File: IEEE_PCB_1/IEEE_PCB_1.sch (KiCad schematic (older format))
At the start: 24 parts, among them U1 555, U2 4017

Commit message: Rev2
Made more changes to the schematic. Will start the footprints soon
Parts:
- added U3: EG1218, symbol IEEE_PCB_Ornament:EG1218
- added U4: 1058TR, symbol IEEE_PCB_Ornament:1058TR
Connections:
- net +3V3: now also U3.1
- net GND: now also U3.3, U4.2 (GND)
- new net: U3.2, U4.1 (PWR)
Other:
- note added: "Clock Circuit"
- note added: "LED circuit"
- note added: "Power"
- moved on the sheet: C1, C2, D1, D2, D3, D4, D5, D6, D7, D8, D9, R1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

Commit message: Footprint assignment
assigned the custom symbols with the custom symbols. Still waiting for standard parts
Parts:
- U1: footprint (none) -> IEEE_PCB_Ornament:555
- U2: footprint (none) -> IEEE_PCB_Ornament:4017
- U3: footprint (none) -> IEEE_PCB_Ornament:EG1218
- U4: footprint (none) -> IEEE_PCB_Ornament:1058TR
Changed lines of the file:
@@
 F 0 "U2" H 3750 3775 50  0000 C CNN
 F 1 "4017" H 3750 3684 50  0000 C CNN
-F 2 "" H 3800 3250 50  0001 C CNN
+F 2 "IEEE_PCB_Ornament:4017" H 3800 3250 50  0001 C CNN
 F 3 "" H 3800 3250 50  0001 C CNN
 	1    3750 3250
@@
 F 0 "U4" H 8750 5500 50  0000 C CNN
 F 1 "1058TR" H 8750 5350 50  0000 C CNN
-F 2 "" H 8750 5400 50  0001 C CNN
+F 2 "IEEE_PCB_Ornament:1058TR" H 8750 5400 50  0001 C CNN
 F 3 "" H 8750 5400 50  0001 C CNN
 	1    8750 5050
@@
 F 0 "U3" V 9254 4522 50  0000 R CNN
 F 1 "EG1218" V 9345 4522 50  0000 R CNN
-F 2 "" H 9300 5000 50  0001 C CNN
+F 2 "IEEE_PCB_Ornament:EG1218" H 9300 5000 50  0001 C CNN
 F 3 "" H 9300 5000 50  0001 C CNN
 	1    9300 4900
@@
 F 0 "U1" H 9250 1965 50  0000 C CNN
 F 1 "555" H 9250 1874 50  0000 C CNN
-F 2 "" H 9200 1150 50  0001 C CNN
+F 2 "IEEE_PCB_Ornament:555" H 9200 1150 50  0001 C CNN
 F 3 "" H 9200 1150 50  0001 C CNN
 	1    9200 1600

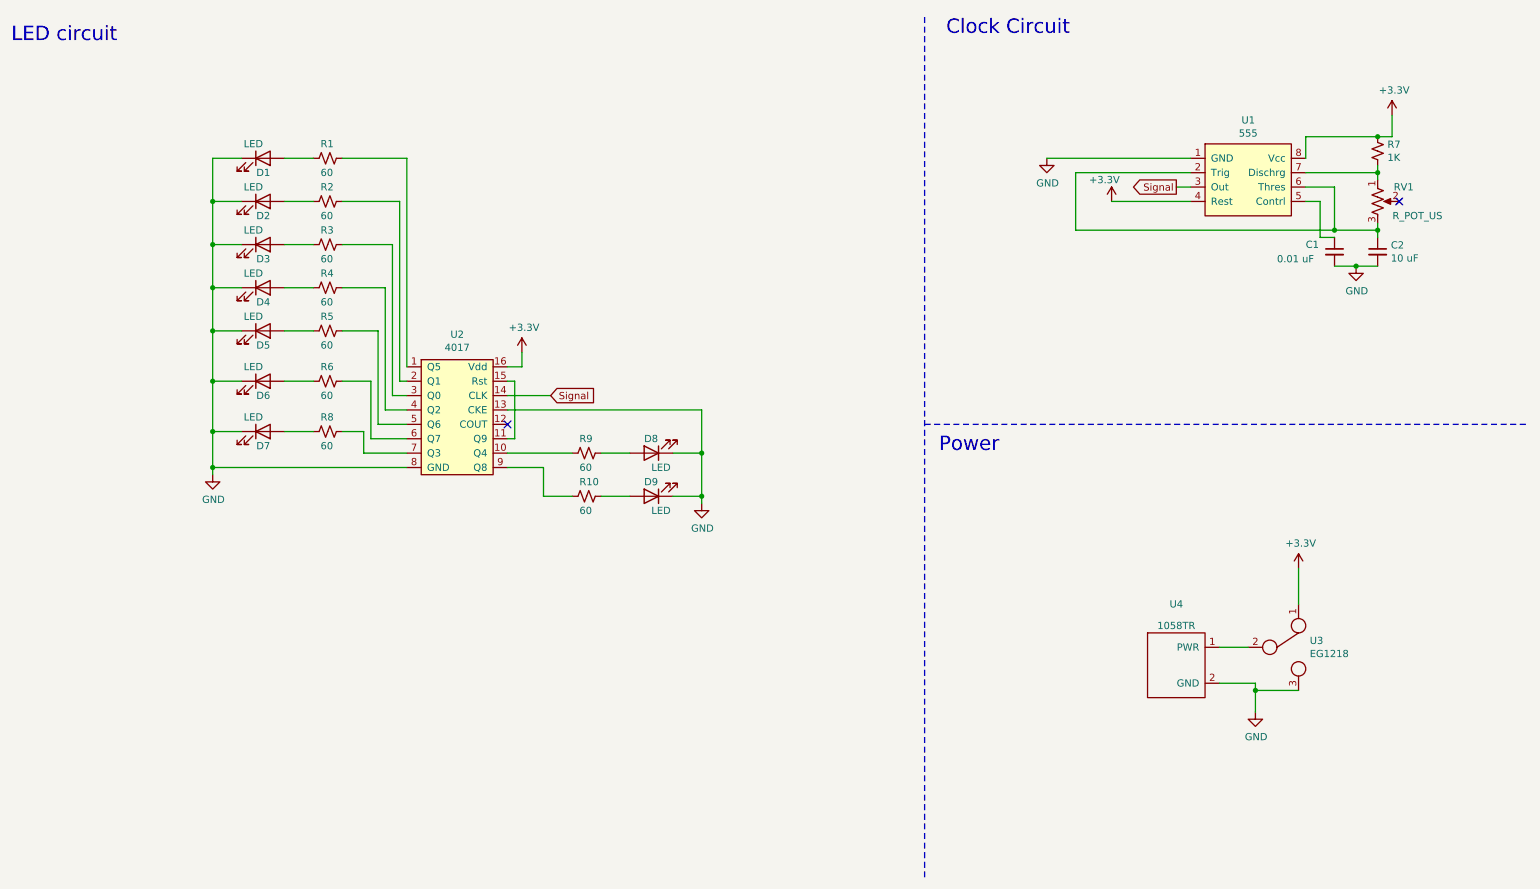
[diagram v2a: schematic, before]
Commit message: Rev3
editted the LEDs
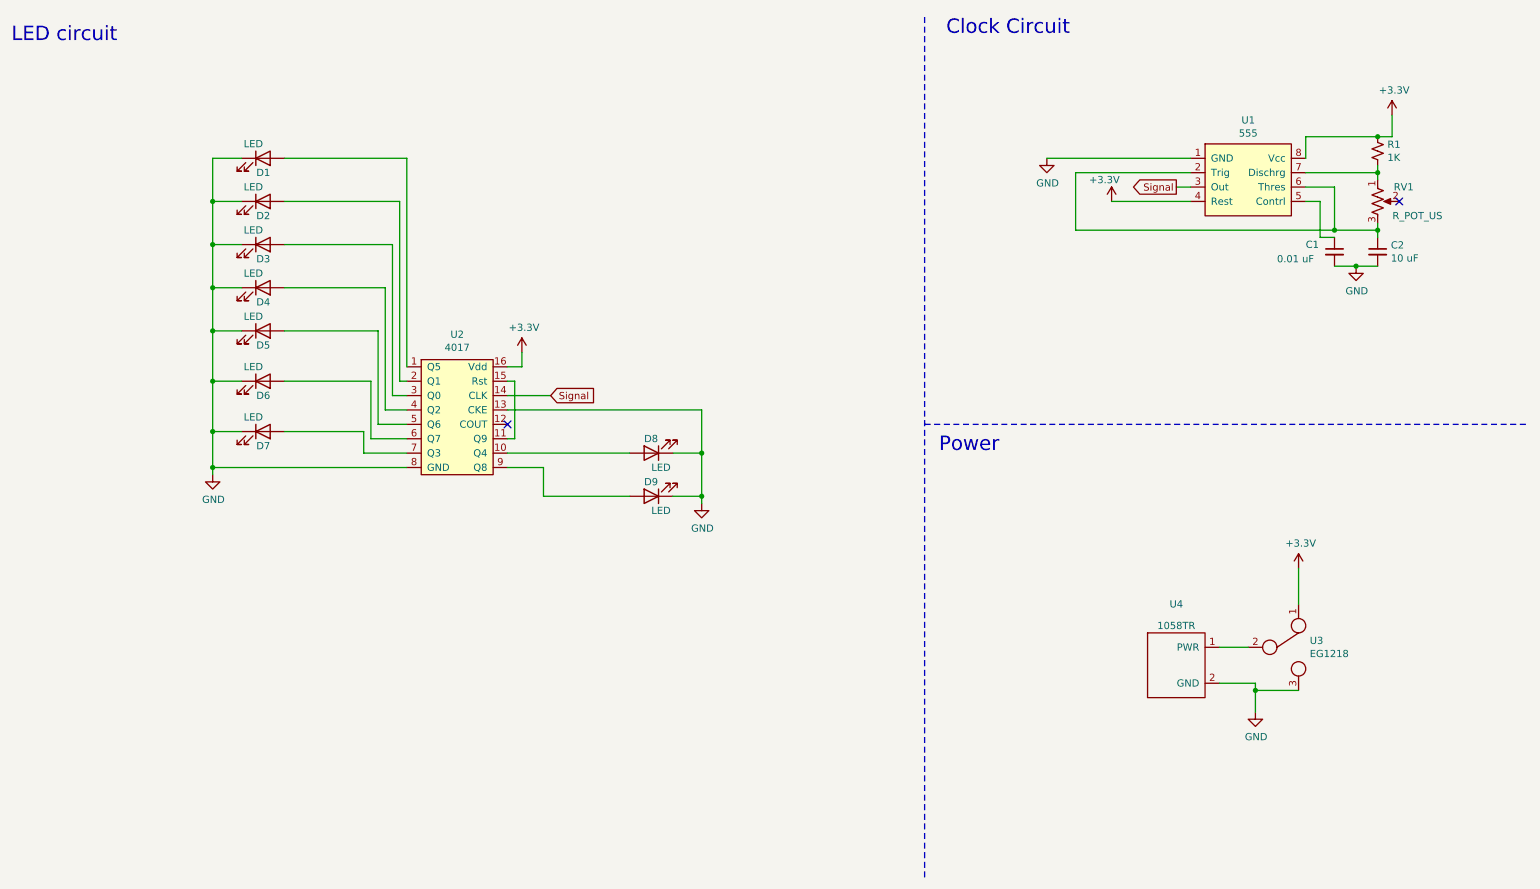
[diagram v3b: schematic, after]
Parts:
- removed R1, R10, R2, R3, R4, R5, R6, R8, R9: 60, symbol Device:R_Small_US
- C1, C2: footprint (none) -> Capacitor_THT:CP_Radial_D5.0mm_P2.00mm
- D1, D2, D3, D4, D5, D6, D7, D8, D9: footprint (none) -> LED_THT:LED_D5.0mm_Clear
- R1: renamed from R7; footprint (none) -> Resistor_THT:R_Axial_DIN0309_L9.0mm_D3.2mm_P12.70mm_Horizontal
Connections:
- net at U2.1 (Q5): now also D1.2 (A)
- net at U2.10 (Q4): now also D8.2 (A)
- net at U2.2 (Q1): now also D2.2 (A)
- net at U2.3 (Q0): now also D3.2 (A)
- net at U2.4 (Q2): now also D4.2 (A)
- net at U2.5 (Q6): now also D5.2 (A)
- net at U2.6 (Q7): now also D6.2 (A)
- net at U2.7 (Q3): now also D7.2 (A)
- net at U2.9 (Q8): now also D9.2 (A)
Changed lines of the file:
@@
 F 0 "D9" H 5150 3750 50  0000 R CNN
 F 1 "LED" H 5100 3950 50  0000 R CNN
-F 2 "" H 5100 3850 50  0001 C CNN
+F 2 "LED_THT:LED_D5.0mm_Clear" H 5100 3850 50  0001 C CNN
 F 3 "~" H 5100 3850 50  0001 C CNN
 	1    5100 3850
@@
 F 0 "D8" H 5150 3450 50  0000 R CNN
 F 1 "LED" H 5100 3650 50  0000 R CNN
-F 2 "" H 5100 3550 50  0001 C CNN
+F 2 "LED_THT:LED_D5.0mm_Clear" H 5100 3550 50  0001 C CNN
 F 3 "~" H 5100 3550 50  0001 C CNN
 	1    5100 3550
@@
 F 0 "D1" H 2450 1400 50  0000 R CNN
 F 1 "LED" H 2400 1600 50  0000 R CNN
-F 2 "" H 2400 1500 50  0001 C CNN
+F 2 "LED_THT:LED_D5.0mm_Clear" H 2400 1500 50  0001 C CNN
 F 3 "~" H 2400 1500 50  0001 C CNN
 	1    2400 1500
@@
 F 0 "D2" H 2450 1700 50  0000 R CNN
 F 1 "LED" H 2400 1900 50  0000 R CNN
-F 2 "" H 2400 1800 50  0001 C CNN
+F 2 "LED_THT:LED_D5.0mm_Clear" H 2400 1800 50  0001 C CNN
 F 3 "~" H 2400 1800 50  0001 C CNN
 	1    2400 1800
@@
 F 0 "D3" H 2450 2000 50  0000 R CNN
 F 1 "LED" H 2400 2200 50  0000 R CNN
-F 2 "" H 2400 2100 50  0001 C CNN
+F 2 "LED_THT:LED_D5.0mm_Clear" H 2400 2100 50  0001 C CNN
 F 3 "~" H 2400 2100 50  0001 C CNN
 	1    2400 2100
@@
 F 0 "D4" H 2450 2300 50  0000 R CNN
 F 1 "LED" H 2400 2500 50  0000 R CNN
-F 2 "" H 2400 2400 50  0001 C CNN
+F 2 "LED_THT:LED_D5.0mm_Clear" H 2400 2400 50  0001 C CNN
 F 3 "~" H 2400 2400 50  0001 C CNN
 	1    2400 2400
@@
 F 0 "D5" H 2450 2600 50  0000 R CNN
 F 1 "LED" H 2400 2800 50  0000 R CNN
-F 2 "" H 2400 2700 50  0001 C CNN
+F 2 "LED_THT:LED_D5.0mm_Clear" H 2400 2700 50  0001 C CNN
 F 3 "~" H 2400 2700 50  0001 C CNN
 	1    2400 2700
@@
 F 0 "D6" H 2450 2950 50  0000 R CNN
 F 1 "LED" H 2400 3150 50  0000 R CNN
-F 2 "" H 2400 3050 50  0001 C CNN
+F 2 "LED_THT:LED_D5.0mm_Clear" H 2400 3050 50  0001 C CNN
 F 3 "~" H 2400 3050 50  0001 C CNN
 	1    2400 3050
@@
 F 0 "D7" H 2450 3300 50  0000 R CNN
 F 1 "LED" H 2400 3500 50  0000 R CNN
-F 2 "" H 2400 3400 50  0001 C CNN
+F 2 "LED_THT:LED_D5.0mm_Clear" H 2400 3400 50  0001 C CNN
 F 3 "~" H 2400 3400 50  0001 C CNN
 	1    2400 3400
 	1    0    0    -1
-$EndComp
-$Comp
-L Device:R_Small_US R1
-U 1 1 62E1ECAF
-P 2850 1500
-F 0 "R1" V 2750 1450 50  0000 L CNN
-F 1 "60" V 2950 1450 50  0000 L CNN
-F 2 "" H 2850 1500 50  0001 C CNN
-F 3 "~" H 2850 1500 50  0001 C CNN
-	1    2850 1500
-	0    1    1    0
-$EndComp
-$Comp
-L Device:R_Small_US R2
-U 1 1 62E1FECC
-P 2850 1800
-F 0 "R2" V 2750 1750 50  0000 L CNN
-F 1 "60" V 2950 1750 50  0000 L CNN
-F 2 "" H 2850 1800 50  0001 C CNN
-F 3 "~" H 2850 1800 50  0001 C CNN
-	1    2850 1800
-	0    1    1    0
-$EndComp
-$Comp
-L Device:R_Small_US R3
-U 1 1 62E2045C
-P 2850 2100
-F 0 "R3" V 2750 2050 50  0000 L CNN
-F 1 "60" V 2950 2050 50  0000 L CNN
-F 2 "" H 2850 2100 50  0001 C CNN
-F 3 "~" H 2850 2100 50  0001 C CNN
-	1    2850 2100
-	0    1    1    0
-$EndComp
-$Comp
-L Device:R_Small_US R4
-U 1 1 62E20C4C
-P 2850 2400
-F 0 "R4" V 2750 2350 50  0000 L CNN
-F 1 "60" V 2950 2350 50  0000 L CNN
-F 2 "" H 2850 2400 50  0001 C CNN
-F 3 "~" H 2850 2400 50  0001 C CNN
-	1    2850 2400
-	0    1    1    0
-$EndComp
-$Comp
-L Device:R_Small_US R5
-U 1 1 62E21420
-P 2850 2700
-F 0 "R5" V 2750 2650 50  0000 L CNN
-F 1 "60" V 2950 2650 50  0000 L CNN
-F 2 "" H 2850 2700 50  0001 C CNN
-F 3 "~" H 2850 2700 50  0001 C CNN
-	1    2850 2700
-	0    1    1    0
-$EndComp
-$Comp
-L Device:R_Small_US R6
-U 1 1 62E21B0F
-P 2850 3050
-F 0 "R6" V 2750 3000 50  0000 L CNN
-F 1 "60" V 2950 3000 50  0000 L CNN
-F 2 "" H 2850 3050 50  0001 C CNN
-F 3 "~" H 2850 3050 50  0001 C CNN
-	1    2850 3050
-	0    1    1    0
-$EndComp
-$Comp
-L Device:R_Small_US R8
-U 1 1 62E223D0
-P 2850 3400
-F 0 "R8" V 2750 3350 50  0000 L CNN
-F 1 "60" V 2950 3350 50  0000 L CNN
-F 2 "" H 2850 3400 50  0001 C CNN
-F 3 "~" H 2850 3400 50  0001 C CNN
-	1    2850 3400
-	0    1    1    0
 $EndComp
 $Comp
@@
 Wire Wire Line
 	2050 3650 2050 3700
-$Comp
-L Device:R_Small_US R9
-U 1 1 62E357AC
-P 4650 3550
-F 0 "R9" V 4550 3500 50  0000 L CNN
-F 1 "60" V 4750 3500 50  0000 L CNN
-F 2 "" H 4650 3550 50  0001 C CNN
-F 3 "~" H 4650 3550 50  0001 C CNN
-	1    4650 3550
-	0    1    1    0
-$EndComp
-$Comp
-L Device:R_Small_US R10
-U 1 1 62E35D4D
-P 4650 3850
-F 0 "R10" V 4550 3800 50  0000 L CNN
-F 1 "60" V 4750 3800 50  0000 L CNN
-F 2 "" H 4650 3850 50  0001 C CNN
-F 3 "~" H 4650 3850 50  0001 C CNN
-	1    4650 3850
-	0    1    1    0
-$EndComp
-Wire Wire Line
-	2950 1500 3400 1500
 Wire Wire Line
 	3400 1500 3400 2950
@@
 	3350 3050 3350 1800
 Wire Wire Line
-	3350 1800 2950 1800
-Wire Wire Line
 	3400 3150 3300 3150
 Wire Wire Line
 	3300 3150 3300 2100
 Wire Wire Line
-	3300 2100 2950 2100
-Wire Wire Line
 	3400 3250 3250 3250
 Wire Wire Line
 	3250 3250 3250 2400
 Wire Wire Line
-	3250 2400 2950 2400
-Wire Wire Line
 	3400 3350 3200 3350
 Wire Wire Line
 	3200 3350 3200 2700
 Wire Wire Line
-	3200 2700 2950 2700
-Wire Wire Line
 	3400 3450 3150 3450
 Wire Wire Line
 	3150 3450 3150 3050
 Wire Wire Line
-	3150 3050 2950 3050
-Wire Wire Line
 	3400 3550 3100 3550
 Wire Wire Line
 	3100 3550 3100 3400
-Wire Wire Line
-	3100 3400 2950 3400
-Wire Wire Line
-	2750 1500 2550 1500
-Wire Wire Line
-	2750 1800 2550 1800
-Wire Wire Line
-	2750 2100 2550 2100
-Wire Wire Line
-	2750 2400 2550 2400
-Wire Wire Line
-	2750 2700 2550 2700
-Wire Wire Line
-	2750 3050 2550 3050
-Wire Wire Line
-	2750 3400 2550 3400
 Wire Wire Line
 	2250 1500 2050 1500
@@
 $EndComp
 Wire Wire Line
-	4750 3550 4950 3550
-Wire Wire Line
-	4100 3550 4550 3550
-Wire Wire Line
 	5250 3550 5450 3550
 Wire Wire Line
@@
 Wire Wire Line
 	4350 3650 4350 3850
-Wire Wire Line
-	4350 3850 4550 3850
-Wire Wire Line
-	4750 3850 4950 3850
 Wire Wire Line
 	5450 3250 5450 3550
@@
 F 0 "C2" H 10242 2196 50  0000 L CNN
 F 1 "10 uF" H 10242 2105 50  0000 L CNN
-F 2 "" H 10150 2150 50  0001 C CNN
+F 2 "Capacitor_THT:CP_Radial_D5.0mm_P2.00mm" H 10150 2150 50  0001 C CNN
 F 3 "~" H 10150 2150 50  0001 C CNN
 	1    10150 2150
@@
 	10150 1350 9650 1350
 $Comp
-L Device:R_Small_US R7
+L Device:R_Small_US R1
 U 1 1 62DE663B
 P 10150 1450
-F 0 "R7" H 10218 1496 50  0000 L CNN
+F 0 "R1" H 10218 1496 50  0000 L CNN
 F 1 "1K" H 10218 1405 50  0000 L CNN
-F 2 "" H 10150 1450 50  0001 C CNN
+F 2 "Resistor_THT:R_Axial_DIN0309_L9.0mm_D3.2mm_P12.70mm_Horizontal" H 10150 1450 50  0001 C CNN
 F 3 "~" H 10150 1450 50  0001 C CNN
 	1    10150 1450
@@
 F 0 "C1" H 9650 2200 50  0000 L CNN
 F 1 "0.01 uF" H 9450 2100 50  0000 L CNN
-F 2 "" H 9850 2150 50  0001 C CNN
+F 2 "Capacitor_THT:CP_Radial_D5.0mm_P2.00mm" H 9850 2150 50  0001 C CNN
 F 3 "~" H 9850 2150 50  0001 C CNN
 	1    9850 2150
@@
 Text Notes 650  700  0    100  ~ 0
 LED circuit
+Wire Wire Line
+	2550 1500 3400 1500
+Wire Wire Line
+	2550 1800 3350 1800
+Wire Wire Line
+	2550 2100 3300 2100
+Wire Wire Line
+	2550 2400 3250 2400
+Wire Wire Line
+	2550 2700 3200 2700
+Wire Wire Line
+	2550 3050 3150 3050
+Wire Wire Line
+	2550 3400 3100 3400
+Wire Wire Line
+	4100 3550 4950 3550
+Wire Wire Line
+	4350 3850 4950 3850
 $EndSCHEMATC
